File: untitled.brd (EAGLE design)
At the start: 53.3 x 44.1 mm, 17 parts

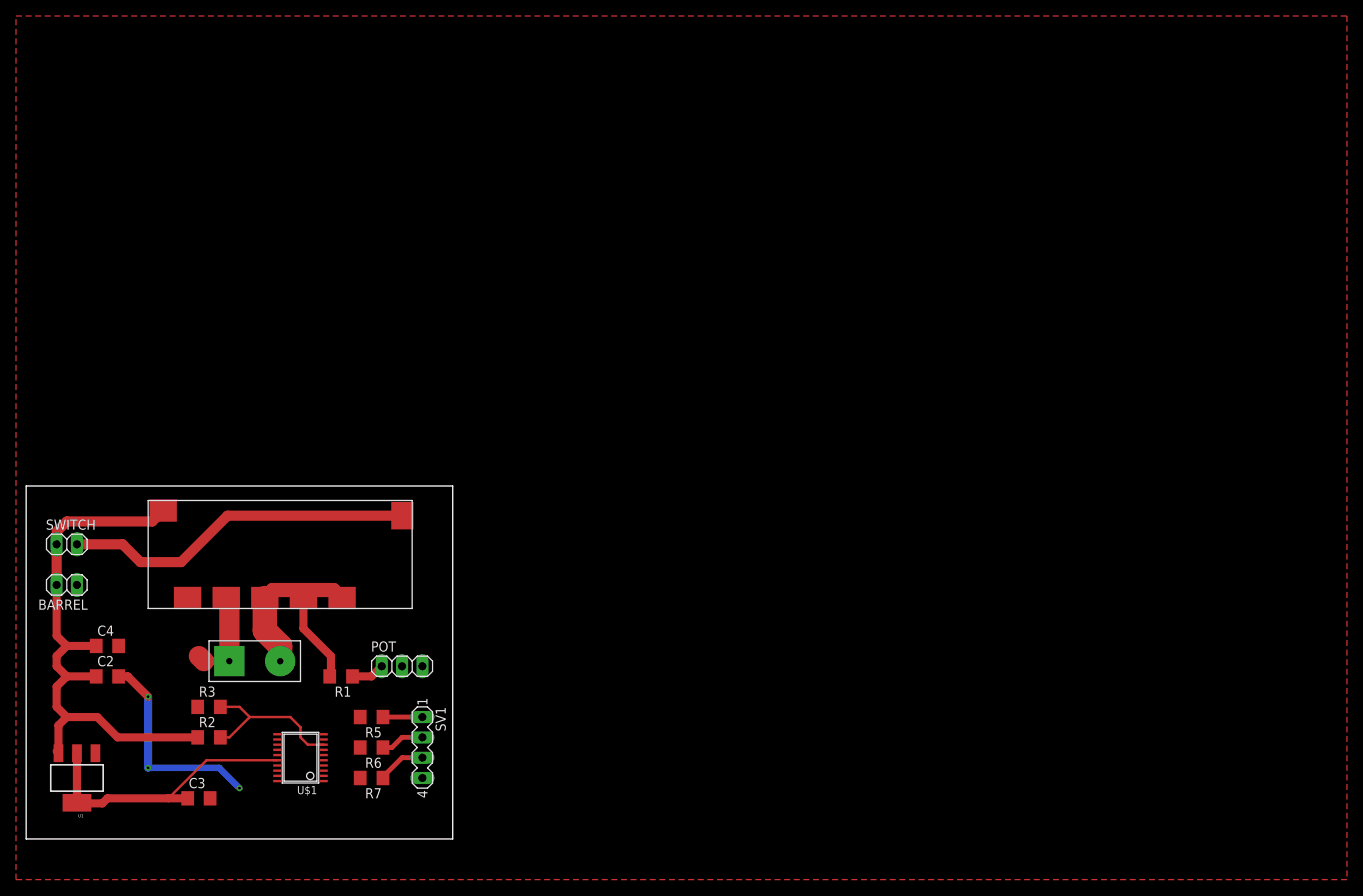
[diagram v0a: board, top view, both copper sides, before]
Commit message: board design done, no DRC errors
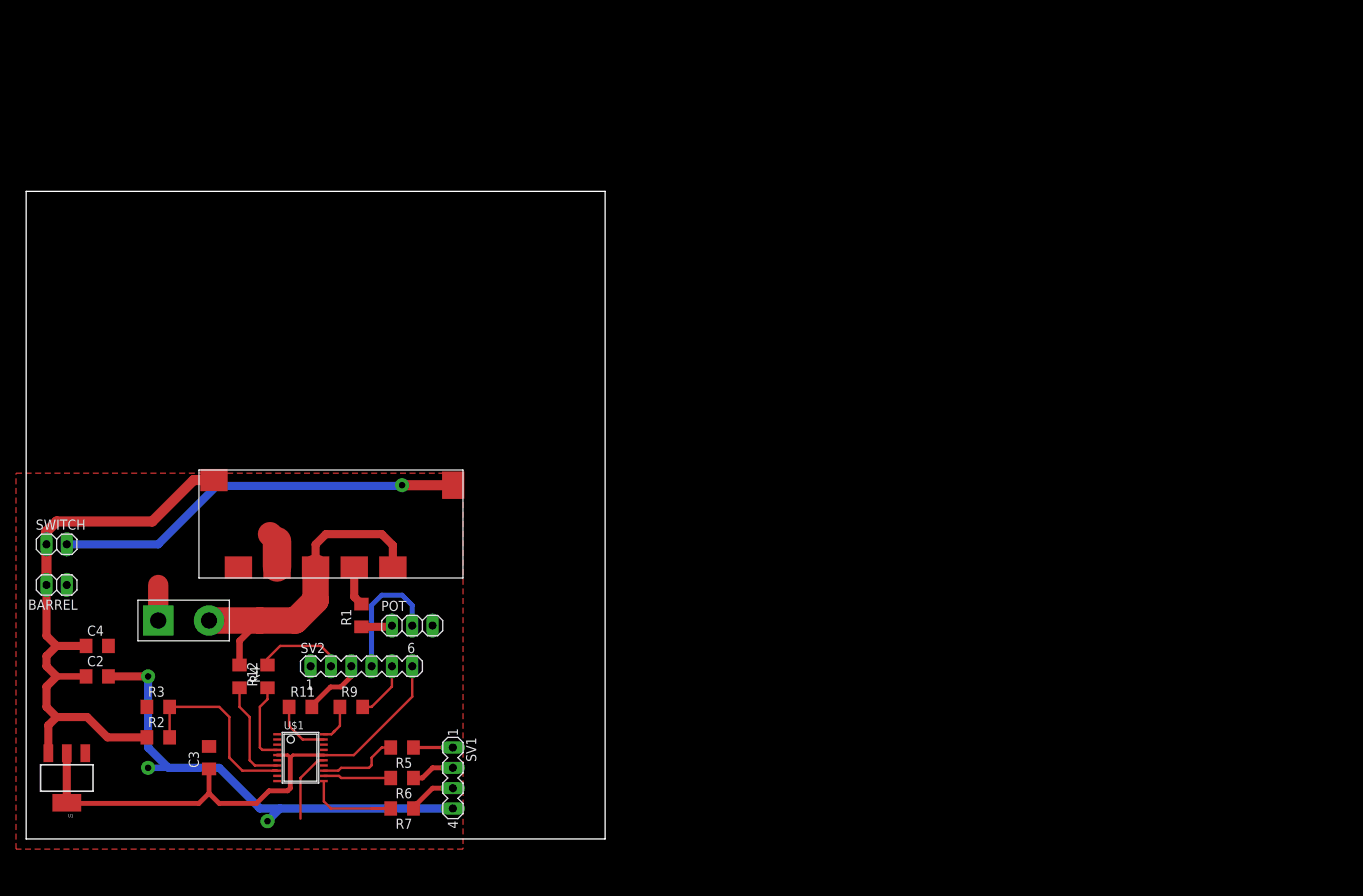
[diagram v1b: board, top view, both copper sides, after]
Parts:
- added R11, R12, R9: 250, rcl:R1206
- added R4: 1k, rcl:R1206
- added SV2: (no value), con-lstb:MA06-1
- R2: value (none) -> 7.5k
- R3: value (none) -> 2.5k
- R5, R6: value (none) -> 250
- R7: value (none) -> 300
- moved POWER 10.2 mm to (19.1, 27.3)
- moved R1 8.03 mm to (41.9, 27.9), turned to 90 degrees
- moved OKY-T/16-D12N-C 7.41 mm to (38.1, 39.4)
- moved R2 6.35 mm to (16.5, 12.7)
- moved R3 6.35 mm to (16.5, 16.5)
- moved R5 5.39 mm to (47.0, 11.4)
- moved R6 5.39 mm to (47.0, 7.62)
- moved R7 5.39 mm to (47.0, 3.81)
- moved SV1 5.39 mm to (53.3, 7.62)
- moved POT 5.24 mm to (48.3, 26.7)
- moved C3 5.24 mm to (22.9, 10.2), turned to 90 degrees
- moved BARREL 1.27 mm to (3.81, 31.8)
- moved SWITCH 1.27 mm to (3.81, 36.8)
- moved C2 1.27 mm to (8.89, 20.3)
- moved C4 1.27 mm to (8.89, 24.1)
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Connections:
- removed net N$2 (its old number): C3.1, U$1.16, U1.2, U1.4
- new net 3V3: C3.1, SV2.6, U$1.16, U$1.5, U1.2, U1.4
- new net N$19: R9.2, SV2.5
- new net N$21: R11.2, SV2.3
- new net N$22: R12.2, SV2.2
- new net N$9: R4.2, U$1.7
- new net NRST: R12.1, U$1.4
- new net SWCLK: R9.1, U$1.20
- new net SWDIO: R11.1, U$1.19
- new net SWO: SV2.1
- net GND: now also SV2.4, U$1.15
- net VOUT: now also R4.1; no longer U$1.7
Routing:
- net 3V3: track 0.00 -> 66.9 mm
- net GND: track 38.2 -> 94.2 mm
- net N$2 (its old number): track 35.9 -> 0.00 mm
- net VOUT: track 19.3 -> 42.4 mm
- net N$9: track 0.00 -> 13.3 mm
- net N$6: track 0.00 -> 11.3 mm
- net N$22: track 0.00 -> 11.2 mm
- net NRST: track 0.00 -> 10.1 mm
- net N$7: track 0.00 -> 10.1 mm
- net N$8: track 0.00 -> 9.17 mm
- net N$21: track 0.00 -> 8.02 mm
- net SWDIO: track 0.00 -> 7.43 mm
- net N$1: track 44.0 -> 51.4 mm, vias 0 -> 1
- net N$19: track 0.00 -> 7.25 mm
- net N$4: track 11.3 -> 4.94 mm
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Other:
- board size 53.3 x 44.1 mm -> 72.4 x 81 mm
